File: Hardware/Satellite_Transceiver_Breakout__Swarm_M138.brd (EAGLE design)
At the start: 35.6 x 88.9 mm, 98 parts, among them Q2 20V/4.2A/52mΩ/1.4W, Q4 20V/4.2A/52mΩ/1.4W, U1 CH340E_MSOP10, U2 SWARM_M138_TRANSCEIVER_MAIN, U3 3.3V

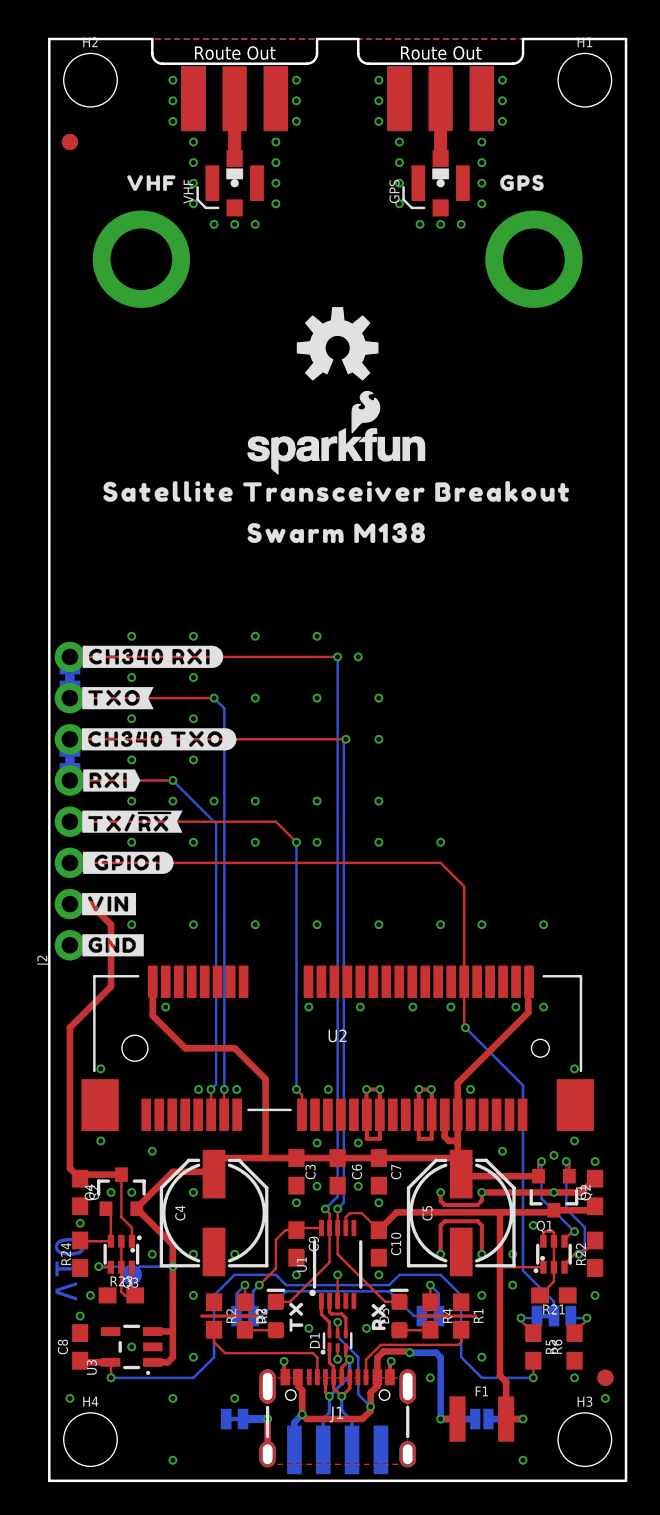
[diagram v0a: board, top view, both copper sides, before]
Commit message: Fixes bottom dimension measurments being off center
* Increases board dimension lines to .008
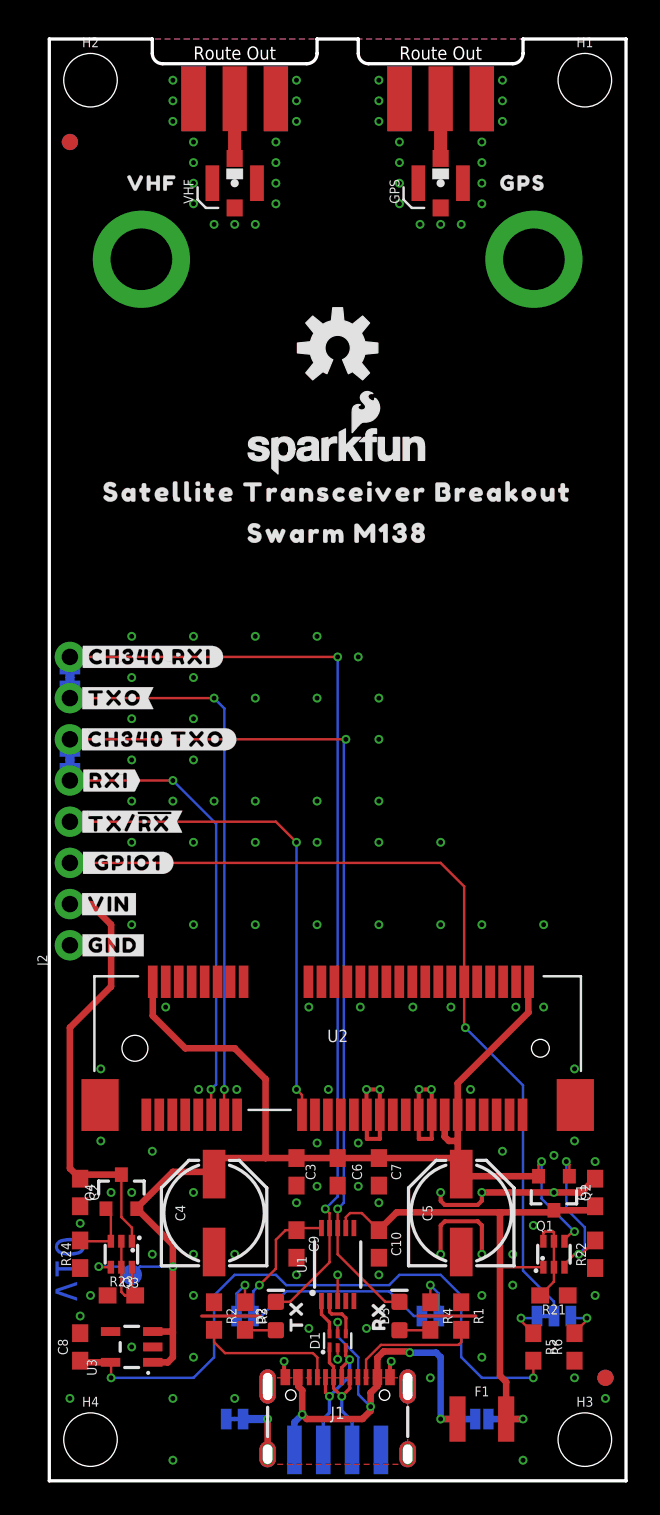
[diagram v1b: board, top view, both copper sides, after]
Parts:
- moved FRAME1 105.3 mm to (71.1, 10.2)
- moved LOGO1 105.3 mm to (43.2, 69.8)
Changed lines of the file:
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@@
 <board>
 <plain>
-<wire x1="0" y1="0" x2="35.56" y2="0" width="0.1524" layer="20"/>
-<wire x1="35.56" y1="0" x2="35.56" y2="88.9" width="0.1524" layer="20"/>
-<wire x1="35.56" y1="88.9" x2="29.21" y2="88.9" width="0.1524" layer="20"/>
-<wire x1="29.21" y1="88.9" x2="29.21" y2="88.011" width="0.1524" layer="20"/>
-<wire x1="29.21" y1="88.011" x2="28.575" y2="87.376" width="0.1524" layer="20" curve="-90"/>
-<wire x1="28.575" y1="87.376" x2="19.685" y2="87.376" width="0.1524" layer="20"/>
-<wire x1="19.685" y1="87.376" x2="19.05" y2="88.011" width="0.1524" layer="20" curve="-90"/>
-<wire x1="19.05" y1="88.011" x2="19.05" y2="88.9" width="0.1524" layer="20"/>
-<wire x1="19.05" y1="88.9" x2="16.51" y2="88.9" width="0.1524" layer="20"/>
-<wire x1="16.51" y1="88.9" x2="16.51" y2="88.011" width="0.1524" layer="20"/>
-<wire x1="16.51" y1="88.011" x2="15.875" y2="87.376" width="0.1524" layer="20" curve="-90"/>
-<wire x1="15.875" y1="87.376" x2="6.985" y2="87.376" width="0.1524" layer="20"/>
-<wire x1="6.985" y1="87.376" x2="6.35" y2="88.011" width="0.1524" layer="20" curve="-90"/>
-<wire x1="6.35" y1="88.011" x2="6.35" y2="88.9" width="0.1524" layer="20"/>
-<wire x1="6.35" y1="88.9" x2="0" y2="88.9" width="0.1524" layer="20"/>
-<wire x1="0" y1="88.9" x2="0" y2="0" width="0.1524" layer="20"/>
-<text x="29.21" y="-68.58" size="1.778" layer="51" font="vector">Paul Clark</text>
+<wire x1="0" y1="0" x2="35.56" y2="0" width="0.2032" layer="20"/>
+<wire x1="35.56" y1="0" x2="35.56" y2="88.9" width="0.2032" layer="20"/>
+<wire x1="35.56" y1="88.9" x2="29.21" y2="88.9" width="0.2032" layer="20"/>
+<wire x1="29.21" y1="88.9" x2="29.21" y2="88.011" width="0.2032" layer="20"/>
+<wire x1="29.21" y1="88.011" x2="28.575" y2="87.376" width="0.2032" layer="20" curve="-90"/>
+<wire x1="28.575" y1="87.376" x2="19.685" y2="87.376" width="0.2032" layer="20"/>
+<wire x1="19.685" y1="87.376" x2="19.05" y2="88.011" width="0.2032" layer="20" curve="-90"/>
+<wire x1="19.05" y1="88.011" x2="19.05" y2="88.9" width="0.2032" layer="20"/>
+<wire x1="19.05" y1="88.9" x2="16.51" y2="88.9" width="0.2032" layer="20"/>
+<wire x1="16.51" y1="88.9" x2="16.51" y2="88.011" width="0.2032" layer="20"/>
+<wire x1="16.51" y1="88.011" x2="15.875" y2="87.376" width="0.2032" layer="20" curve="-90"/>
+<wire x1="15.875" y1="87.376" x2="6.985" y2="87.376" width="0.2032" layer="20"/>
+<wire x1="6.985" y1="87.376" x2="6.35" y2="88.011" width="0.2032" layer="20" curve="-90"/>
+<wire x1="6.35" y1="88.011" x2="6.35" y2="88.9" width="0.2032" layer="20"/>
+<wire x1="6.35" y1="88.9" x2="0" y2="88.9" width="0.2032" layer="20"/>
+<wire x1="0" y1="88.9" x2="0" y2="0" width="0.2032" layer="20"/>
+<text x="99.06" y="10.16" size="1.778" layer="51" font="vector">Paul Clark</text>
 <rectangle x1="10.668" y1="79.121" x2="12.192" y2="80.899" layer="41"/>
 <rectangle x1="23.368" y1="79.121" x2="24.892" y2="80.899" layer="41"/>
-<text x="-24.13" y="-20.32" size="1.778" layer="51" font="vector" ratio="15" align="top-left">2-Layer Board
+<text x="45.72" y="58.42" size="1.778" layer="51" font="vector" ratio="15" align="top-left">2-Layer Board
 1.6mm Thickness
 1oz Copper
@@
 </text>
 <text x="2.159" y="13.081" size="1.778" layer="16" font="vector" ratio="15" rot="MR270" align="bottom-center">v10</text>
-<dimension x1="-0.508" y1="0" x2="35.052" y2="0" x3="17.272" y3="-12.7" textsize="1.778" textratio="15" layer="47" dtype="horizontal" unit="inch"/>
-<dimension x1="2.032" y1="2.54" x2="32.512" y2="2.54" x3="17.272" y3="-8.89" textsize="1.778" textratio="15" layer="47" dtype="horizontal" unit="inch"/>
 <dimension x1="0" y1="88.9" x2="0" y2="0" x3="-11.43" y3="44.45" textsize="1.778" textratio="15" layer="47" dtype="vertical" unit="inch"/>
 <dimension x1="2.54" y1="86.36" x2="2.54" y2="2.54" x3="-3.81" y3="44.45" textsize="1.778" textratio="15" layer="47" dtype="vertical" unit="inch"/>
@@
 <wire x1="17.8181" y1="3.429" x2="17.8181" y2="0.381" width="0.0762" layer="42"/>
 <wire x1="19.5961" y1="3.429" x2="19.5961" y2="0.381" width="0.0762" layer="42"/>
-<text x="12.7" y="-71.12" size="1.778" layer="51" font="vector">Revised By: Elias Santistevan</text>
+<text x="82.55" y="7.62" size="1.778" layer="51" font="vector">Revised By: Elias Santistevan</text>
 <dimension x1="11.43" y1="86.36" x2="0" y2="86.36" x3="5.715" y3="97.79" textsize="1.778" layer="47" unit="inch"/>
 <dimension x1="24.13" y1="85.217" x2="35.56" y2="85.217" x3="29.845" y3="97.79" textsize="1.778" layer="47" unit="inch"/>
 <dimension x1="33.02" y1="86.36" x2="35.56" y2="86.36" x3="34.29" y3="91.44" textsize="1.778" layer="47" unit="inch"/>
 <dimension x1="2.54" y1="86.36" x2="2.54" y2="88.9" x3="-3.81" y3="87.63" textsize="1.778" layer="47" unit="inch"/>
-<dimension x1="17.78" y1="6.731" x2="0" y2="6.731" x3="8.89" y3="-3.81" textsize="1.778" layer="47" unit="inch"/>
+<dimension x1="17.78" y1="6.731" x2="0" y2="6.731" x3="8.89" y3="-5.08" textsize="1.778" layer="47" unit="inch"/>
+<dimension x1="35.56" y1="0" x2="0" y2="0" x3="17.78" y3="-15.24" textsize="1.778" textratio="15" layer="47" unit="inch"/>
+<dimension x1="2.54" y1="2.54" x2="33.02" y2="2.54" x3="17.78" y3="-10.16" textsize="1.778" textratio="15" layer="47" unit="inch"/>
 </plain>
 <attributes>
@@
 </autorouter>
 <elements>
-<element name="FRAME1" library="SparkFun-Aesthetics" package="CREATIVE_COMMONS" value="FRAME-LEDGER" x="1.27" y="-68.58" smashed="yes">
-<attribute name="DESIGNER" value="" x="1.27" y="-68.58" size="1.778" layer="27" font="vector" ratio="15" display="off"/>
-<attribute name="REV" value="" x="1.27" y="-68.58" size="1.778" layer="27" font="vector" ratio="15" display="off"/>
+<element name="FRAME1" library="SparkFun-Aesthetics" package="CREATIVE_COMMONS" value="FRAME-LEDGER" x="71.12" y="10.16" smashed="yes">
+<attribute name="DESIGNER" value="" x="71.12" y="10.16" size="1.778" layer="27" font="vector" ratio="15" display="off"/>
+<attribute name="REV" value="" x="71.12" y="10.16" size="1.778" layer="27" font="vector" ratio="15" display="off"/>
 </element>
-<element name="LOGO1" library="SparkFun-Aesthetics" package="ORDERING_INSTRUCTIONS" value="SPECIAL_INSTRUCTIONS-ORDERING" x="-26.67" y="-8.89" smashed="yes"/>
+<element name="LOGO1" library="SparkFun-Aesthetics" package="ORDERING_INSTRUCTIONS" value="SPECIAL_INSTRUCTIONS-ORDERING" x="43.18" y="69.85" smashed="yes"/>
 <element name="FD1" library="SparkFun-Aesthetics" package="FIDUCIAL-1X2" value="FIDUCIAL1X2" x="34.29" y="6.35" smashed="yes"/>
 <element name="FD2" library="SparkFun-Aesthetics" package="FIDUCIAL-1X2" value="FIDUCIAL1X2" x="34.29" y="6.35" smashed="yes" rot="MR0"/>
